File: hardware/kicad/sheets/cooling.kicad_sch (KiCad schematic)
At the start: 22 parts, among them J3 FAN (4-pin PWM), J4 PUMP (4-pin PWM), J5 ALPHACOOL ES FLOW (3-pin), J6 ALPHACOOL ES NTC 10k, U10 EMC2303-x-KP

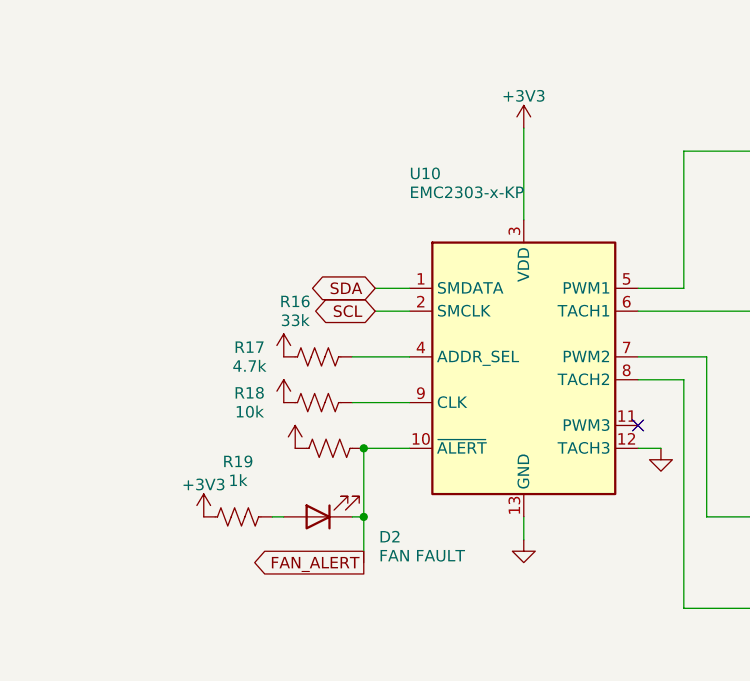
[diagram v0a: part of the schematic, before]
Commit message: Put supply pins on top and grounds on the bottom of IC symbols; flake8-clean Python
Schematic: re-laid out pins on U2, U3, U6, U7, U11, U14, U17-U20, U22-U24
and PS1 (supply on top, ground/strap pins on the bottom edge) via custom
`cryocooler:` symbols (make_lib.from_stock) and a gnd_bus helper; U18/U2
use mirroring instead of a 180 degree rotation. Nets are unchanged (ERC 0,
117/117 datasheet rules, PCB nets still match). Text placement now shows
every power-symbol name, avoids wires, and uses a realistic character width.

Python: black -l 79 -S plus manual wrapping so hardware/kicad and scripts/
pass flake8; add .flake8.

Co-Authored-By: Claude Sonnet 5.5 <noreply@anthropic.com>
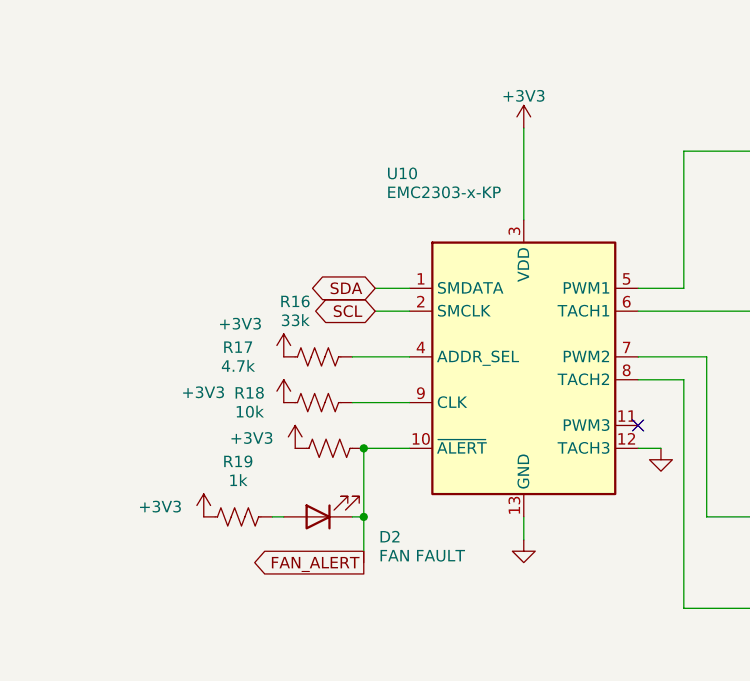
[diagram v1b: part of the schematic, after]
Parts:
- removed C28: 100nF, Capacitor_SMD:C_0603_1608Metric, symbol Device:C
- removed D2: FAN FAULT, LED_SMD:LED_0603_1608Metric, symbol Device:LED
- removed J3: FAN (4-pin PWM), Connector_Molex:Molex_KK-254_AE-6410-04A_1x04_P2.54mm_Vertical, symbol Connector_Generic:Conn_01x04
- removed R21, R23: 4.7k, Resistor_SMD:R_0603_1608Metric, symbol Device:R_US
- removed R25: 10k, Resistor_SMD:R_0603_1608Metric, symbol Device:R_US
- added C25: 100nF, Capacitor_SMD:C_0603_1608Metric, symbol Device:C
- added J5: ALPHACOOL ES FLOW (3-pin), Connector_Molex:Molex_KK-254_AE-6410-03A_1x03_P2.54mm_Vertical, symbol Connector_Generic:Conn_01x03
- added R19: 1k, Resistor_SMD:R_0603_1608Metric, symbol Device:R_US
- added R20, R22, R26: 10k, Resistor_SMD:R_0603_1608Metric, symbol Device:R_US
- C28: renamed from R26; value 10k -> 100nF; footprint Resistor_SMD:R_0603_1608Metric -> Capacitor_SMD:C_0603_1608Metric; symbol Device:R_US -> Device:C
- D2: renamed from R18; value 10k -> FAN FAULT; footprint Resistor_SMD:R_0603_1608Metric -> LED_SMD:LED_0603_1608Metric; symbol Device:R_US -> Device:LED
- J3: renamed from R19; value 1k -> FAN (4-pin PWM); footprint Resistor_SMD:R_0603_1608Metric -> Connector_Molex:Molex_KK-254_AE-6410-04A_1x04_P2.54mm_Vertical; symbol Device:R_US -> Connector_Generic:Conn_01x04
- R16: renamed from C25; value 100nF -> 33k; footprint Capacitor_SMD:C_0603_1608Metric -> Resistor_SMD:R_0603_1608Metric; symbol Device:C -> Device:R_US
- R17: renamed from R16; value 33k -> 4.7k
- R18: renamed from R17; value 4.7k -> 10k
- R21: renamed from R20; value 10k -> 4.7k
- R23: renamed from R22; value 10k -> 4.7k
- R25: renamed from J5; value ALPHACOOL ES FLOW (3-pin) -> 10k; footprint Connector_Molex:Molex_KK-254_AE-6410-03A_1x03_P2.54mm_Vertical -> Resistor_SMD:R_0603_1608Metric; symbol Connector_Generic:Conn_01x03 -> Device:R_US
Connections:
- net +12V: now also J3.2 (Pin_2), J5.2 (Pin_2); no longer R25.2 (Pin_2)
- net +3V3: now also R25.1, C25.1, R19.1, R20.1, R22.1, R26.1; no longer C28.1, D2.1, J3.1
- net FAN_ALERT: now also D2.1 (K), R18.2; no longer D2.2
- net FLOW_TACH: now also R25.2
- net GND: now also C28.2, J3.1 (Pin_1), C25.2, J5.1 (Pin_1); no longer R16.2, R25.1 (Pin_1)
- net NTC_ADC: now also C28.1, R26.2; no longer C28.2
- net at R24.2: now also J5.3 (Pin_3); no longer R25.3 (Pin_3)
- net at R21.2: now also J3.3 (Pin_3), U10.6 (TACH1); no longer U10.5 (PWM1)
- net at U10.4 (ADDR_SEL): now also R16.2; no longer R17.2
- net at J4.4 (Pin_4), U10.7 (PWM2): now also R22.2; no longer R23.2
- net at J4.3 (Pin_3), U10.8 (TACH2): now also R23.2
- net at U10.9 (CLK): now also R17.2; no longer R18.2
- new net: D2.2 (A), R19.2
- new net: J3.4 (Pin_4), R20.2, U10.5 (PWM1)
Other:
- moved on the sheet: D2, R17, R18, R21, R23

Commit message: KiCad schematic: INA239, ADS1220, SC18IS604 bridge, relay driver, test points
- system_current: INA237 -> INA239 (SPI, CS GPIO3) with the 49.9 ohm / 470 nF
  input filter, power LED and ALERT LED; VBUS shares the filtered IN- node.
- cold_head: ADS122C04 -> ADS1220 (SPI, CS GPIO44).
- i2c_bridge (new): SC18IS604 SPI-to-I2C bridge for the EMC2303, with a
  74LVC1G125 gating its MISO onto the shared bus.
- compressor_relay (new): GPIO16 high-side switch sharing one generator
  function with the amplifier REM switch.
- debug (new): about 40 test points and rail LEDs (the isolated rail LED
  returns to ISO_GND).
- ISO7741 -> ACS37800 SPI lines are straight wires (pins reordered on the
  symbol); USB_VBUS is one wire plus a naming label.
- Custom symbols for INA239, ADS1220, SC18IS604; datasheet rules 117 -> 162;
  GPIO map checks updated. ERC 0.

Co-Authored-By: Claude Sonnet 5.5 <noreply@anthropic.com>
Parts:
- removed C24: 1uF, Capacitor_SMD:C_0805_2012Metric, symbol Device:C
- removed J5: ALPHACOOL ES FLOW (3-pin), Connector_Molex:Molex_KK-254_AE-6410-03A_1x03_P2.54mm_Vertical, symbol Connector_Generic:Conn_01x03
- removed J6: ALPHACOOL ES NTC 10k, Connector_JST:JST_XH_B2B-XH-A_1x02_P2.50mm_Vertical, symbol Connector_Generic:Conn_01x02
- removed R18, R20, R26: 10k, Resistor_SMD:R_0603_1608Metric, symbol Device:R_US
- added C25: 100nF, Capacitor_SMD:C_0603_1608Metric, symbol Device:C
- added C26, C27: 22uF/25V, Capacitor_SMD:C_1210_3225Metric, symbol Device:C
- added R14: 33k, Resistor_SMD:R_0603_1608Metric, symbol Device:R_US
- added R17: 1k, Resistor_SMD:R_0603_1608Metric, symbol Device:R_US
- added U10: EMC2303-x-KP, Package_DFN_QFN:VQFN-12-1EP_4x4mm_P0.8mm_EP2.1x2.1mm_ThermalVias, symbol Driver_Motor:EMC2303-x-KP
- C24: renamed from U10; value EMC2303-x-KP -> 1uF; footprint Package_DFN_QFN:VQFN-12-1EP_4x4mm_P0.8mm_EP2.1x2.1mm_ThermalVias -> Capacitor_SMD:C_0805_2012Metric; symbol Driver_Motor:EMC2303-x-KP -> Device:C
- D2: renamed from R17; value 4.7k -> FAN FAULT; footprint Resistor_SMD:R_0603_1608Metric -> LED_SMD:LED_0603_1608Metric; symbol Device:R_US -> Device:LED
- J5: renamed from C27; value 22uF/25V -> ALPHACOOL ES FLOW (3-pin); footprint Capacitor_SMD:C_1210_3225Metric -> Connector_Molex:Molex_KK-254_AE-6410-03A_1x03_P2.54mm_Vertical; symbol Device:C -> Connector_Generic:Conn_01x03
- J6: renamed from R25; value 10k -> ALPHACOOL ES NTC 10k; footprint Resistor_SMD:R_0603_1608Metric -> Connector_JST:JST_XH_B2B-XH-A_1x02_P2.50mm_Vertical; symbol Device:R_US -> Connector_Generic:Conn_01x02
- R15: renamed from C25; value 100nF -> 4.7k; footprint Capacitor_SMD:C_0603_1608Metric -> Resistor_SMD:R_0603_1608Metric; symbol Device:C -> Device:R_US
- R16: value 33k -> 10k
- R18: renamed from D2; value FAN FAULT -> 10k; footprint LED_SMD:LED_0603_1608Metric -> Resistor_SMD:R_0603_1608Metric; symbol Device:LED -> Device:R_US
- R19: value 1k -> 4.7k
- R20: renamed from C26; value 22uF/25V -> 10k; footprint Capacitor_SMD:C_1210_3225Metric -> Resistor_SMD:R_0603_1608Metric; symbol Device:C -> Device:R_US
- R22: value 10k -> 1k
- R23: value 4.7k -> 10k
- R24: value 1k -> 10k
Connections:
- net +12V: now also J5.2 (Pin_2), C26.1, C27.1; no longer J5.1, R20.1
- net +3V3: now also C24.1, R18.1, R20.1, R24.1, C25.1, R14.1, R17.1, U10.3 (VDD); no longer C24.3 (VDD), D2.1, J6.1, R22.1
- net FAN_ALERT: now also D2.1 (K), R16.2, U10.10 (~{ALERT}); no longer C24.10 (~{ALERT}), R18.1 (K)
- net FLOW_TACH: now also R22.1, R23.2; no longer J6.2, R24.1
- net GND: now also C24.2, J5.1 (Pin_1), J6.2 (Pin_2), C25.2, C26.2, C27.2, U10.12 (TACH3), U10.13 (GND); no longer C24.12 (TACH3), C24.13 (GND), J5.2, R15.2, R20.2
- net NTC_ADC: now also J6.1 (Pin_1), R24.2
- net SCL: now also U10.2 (SMCLK); no longer C24.2 (SMCLK)
- net SDA: now also U10.1 (SMDATA); no longer C24.1 (SMDATA)
- net at R19.2: now also J3.3 (Pin_3), U10.6 (TACH1); no longer R18.2 (A)
- net at J3.4 (Pin_4): now also R18.2, U10.5 (PWM1); no longer C24.5 (PWM1)
- net at D2.2 (A): now also R17.2; no longer C24.9 (CLK)
- new net: J4.3 (Pin_3), R21.2, U10.8 (TACH2)
- new net: J4.4 (Pin_4), R20.2, U10.7 (PWM2)
- new net: J5.3 (Pin_3), R22.2
- new net: R14.2, U10.4 (ADDR_SEL)
- new net: R15.2, U10.9 (CLK)
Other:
- moved on the sheet: D2, R16, R18

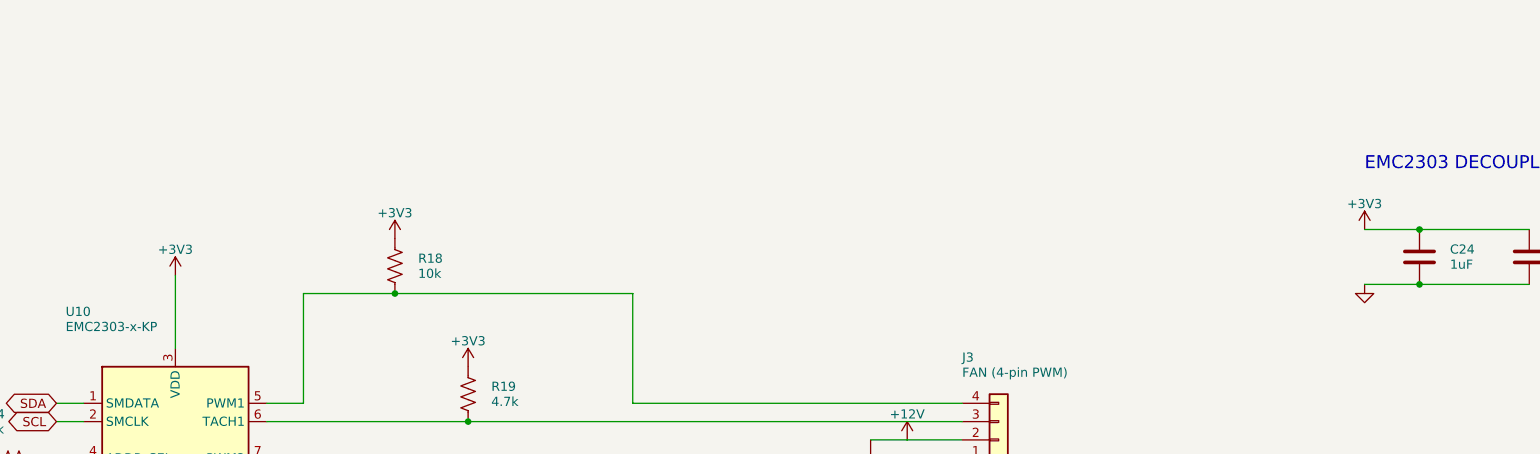
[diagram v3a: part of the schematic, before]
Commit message: Add per-section supply jumpers, 8-pin IMU header and connector pin labels
- Four 1.27 mm 2-pin jumpers (JP1-JP4), each with a rail-on LED, cut the
  supply of one section for debugging: signal generator +3V3, +-15V
  generator +5V in, isolated amp-current supply +5V in, and a shared
  +3V3 net for the cooling chips (EMC2303, RTD ADC, I2C bridge).
- J14 is now an 8-pin JST XH in the Adafruit LSM6DSOX pad order
  (VIN, GND, SCL, SDA, DO, CS, I1, I2); firmware pin comments updated.
- Pin-function labels beside every connector, "RAILS ±15V" box title.
- Board re-placed and re-routed (130 x 110 mm); DRC 0 errors, 0 unconnected,
  ERC 0, 173 datasheet rules pass. BOM, READMEs, Gerbers and renders
  regenerated; link_usb_vbus.py now adapts to the routed layout.

Co-Authored-By: Claude Sonnet 5.5 <noreply@anthropic.com>
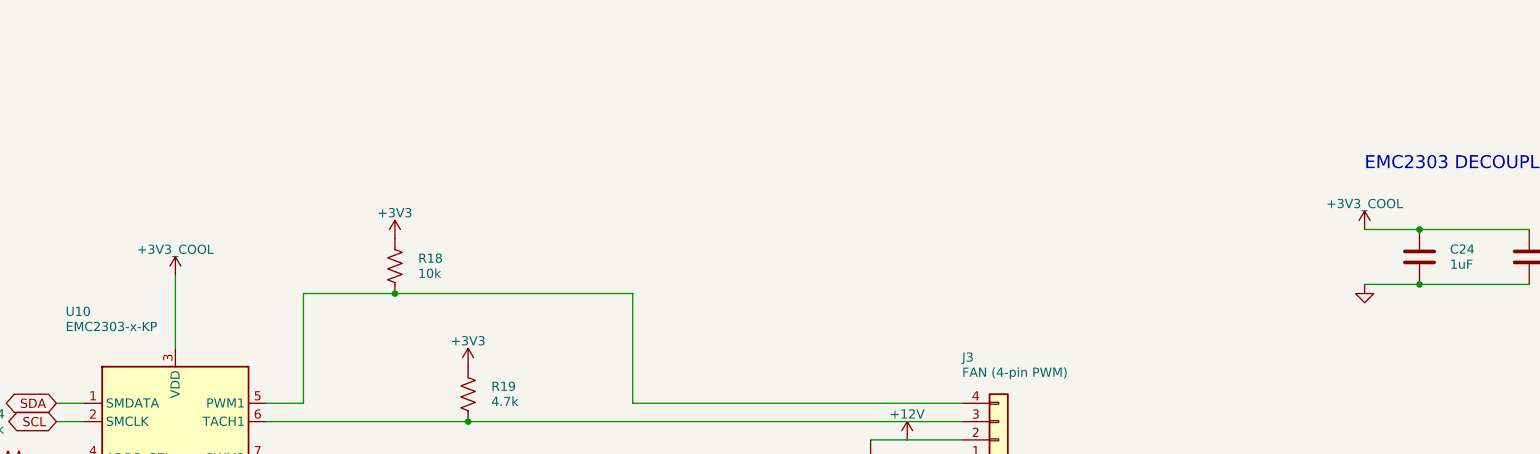
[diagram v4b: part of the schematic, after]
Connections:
- net +3V3: no longer C24.1, C25.1, U10.3 (VDD)
- new net +3V3_COOL: C24.1, C25.1, U10.3 (VDD)
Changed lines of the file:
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@@
 	)
 	(junction
-		(at 106.68 190.5)
+		(at 132.08 116.84)
 		(diameter 0)
 		(color 0 0 0 0)
 	)
 	(junction
-		(at 132.08 116.84)
+		(at 106.68 190.5)
 		(diameter 0)
 		(color 0 0 0 0)
 	)
 	(junction
-		(at 106.68 66.04)
+		(at 58.42 106.68)
 		(diameter 0)
 		(color 0 0 0 0)
 	)
 	(junction
-		(at 116.84 83.82)
+		(at 248.92 57.15)
 		(diameter 0)
 		(color 0 0 0 0)
 	)
 	(junction
-		(at 248.92 57.15)
+		(at 58.42 99.06)
 		(diameter 0)
 		(color 0 0 0 0)
 	)
 	(junction
-		(at 58.42 106.68)
+		(at 248.92 64.77)
 		(diameter 0)
 		(color 0 0 0 0)
 	)
 	(junction
-		(at 114.3 106.68)
+		(at 109.22 160.02)
 		(diameter 0)
 		(color 0 0 0 0)
 	)
 	(junction
-		(at 58.42 99.06)
+		(at 116.84 83.82)
 		(diameter 0)
 		(color 0 0 0 0)
 	)
 	(junction
-		(at 109.22 160.02)
+		(at 106.68 66.04)
 		(diameter 0)
 		(color 0 0 0 0)
 	)
 	(junction
-		(at 116.84 190.5)
+		(at 114.3 106.68)
 		(diameter 0)
 		(color 0 0 0 0)
 	)
 	(junction
-		(at 248.92 64.77)
+		(at 116.84 190.5)
 		(diameter 0)
 		(color 0 0 0 0)
@@
 	(wire
 		(pts
-			(xy 152.4 114.3) (xy 185.42 114.3)
+			(xy 93.98 116.84) (xy 132.08 116.84)
 		)
 		(stroke
@@
 	(wire
 		(pts
-			(xy 59.69 81.28) (xy 63.5 81.28)
+			(xy 152.4 114.3) (xy 185.42 114.3)
 		)
 		(stroke
@@
 	(wire
 		(pts
-			(xy 172.72 119.38) (xy 177.8 119.38)
+			(xy 116.84 190.5) (xy 134.62 190.5)
 		)
 		(stroke
@@
 	(wire
 		(pts
-			(xy 241.3 57.15) (xy 248.92 57.15)
+			(xy 109.22 160.02) (xy 119.38 160.02)
 		)
 		(stroke
@@
 	(wire
 		(pts
-			(xy 182.88 88.9) (xy 185.42 88.9)
+			(xy 248.92 57.15) (xy 264.16 57.15)
 		)
 		(stroke
@@
 	(wire
 		(pts
-			(xy 127 160.02) (xy 134.62 160.02)
+			(xy 116.84 83.82) (xy 185.42 83.82)
 		)
 		(stroke
@@
 	(wire
 		(pts
-			(xy 76.2 106.68) (xy 76.2 109.22)
+			(xy 93.98 66.04) (xy 93.98 81.28)
 		)
 		(stroke
@@
 	(wire
 		(pts
-			(xy 182.88 121.92) (xy 185.42 121.92)
+			(xy 76.2 106.68) (xy 76.2 109.22)
 		)
 		(stroke
@@
 	(wire
 		(pts
-			(xy 124.46 154.94) (xy 134.62 154.94)
+			(xy 58.42 99.06) (xy 58.42 106.68)
 		)
 		(stroke
@@
 	(wire
 		(pts
-			(xy 58.42 99.06) (xy 63.5 99.06)
+			(xy 248.92 64.77) (xy 264.16 64.77)
 		)
 		(stroke
@@
 	(wire
 		(pts
-			(xy 114.3 106.68) (xy 152.4 106.68)
+			(xy 96.52 190.5) (xy 106.68 190.5)
 		)
 		(stroke
@@
 	(wire
 		(pts
-			(xy 109.22 160.02) (xy 119.38 160.02)
+			(xy 58.42 106.68) (xy 58.42 111.76)
 		)
 		(stroke
@@
 	(wire
 		(pts
-			(xy 139.7 66.04) (xy 139.7 81.28)
+			(xy 241.3 57.15) (xy 248.92 57.15)
 		)
 		(stroke
@@
 	(wire
 		(pts
-			(xy 116.84 190.5) (xy 134.62 190.5)
+			(xy 93.98 91.44) (xy 93.98 116.84)
 		)
 		(stroke
@@
 	(wire
 		(pts
-			(xy 152.4 106.68) (xy 152.4 114.3)
+			(xy 58.42 99.06) (xy 63.5 99.06)
 		)
 		(stroke
@@
 	(wire
 		(pts
-			(xy 129.54 157.48) (xy 134.62 157.48)
+			(xy 139.7 81.28) (xy 185.42 81.28)
 		)
 		(stroke
@@
 	(wire
 		(pts
-			(xy 96.52 106.68) (xy 114.3 106.68)
+			(xy 152.4 106.68) (xy 152.4 114.3)
 		)
 		(stroke
@@
 	(wire
 		(pts
-			(xy 241.3 64.77) (xy 248.92 64.77)
+			(xy 48.26 106.68) (xy 49.53 106.68)
 		)
 		(stroke
@@
 	(wire
 		(pts
-			(xy 88.9 99.06) (xy 91.44 99.06)
+			(xy 241.3 64.77) (xy 248.92 64.77)
 		)
 		(stroke
@@
 	(wire
 		(pts
-			(xy 93.98 66.04) (xy 106.68 66.04)
+			(xy 177.8 86.36) (xy 185.42 86.36)
 		)
 		(stroke
@@
 	(wire
 		(pts
-			(xy 76.2 63.5) (xy 76.2 73.66)
+			(xy 124.46 154.94) (xy 134.62 154.94)
 		)
 		(stroke
@@
 	(wire
 		(pts
-			(xy 106.68 190.5) (xy 116.84 190.5)
+			(xy 114.3 106.68) (xy 152.4 106.68)
 		)
 		(stroke
@@
 	(wire
 		(pts
-			(xy 88.9 81.28) (xy 93.98 81.28)
+			(xy 57.15 106.68) (xy 58.42 106.68)
 		)
 		(stroke
@@
 	(wire
 		(pts
-			(xy 59.69 83.82) (xy 63.5 83.82)
+			(xy 88.9 83.82) (xy 116.84 83.82)
 		)
 		(stroke
@@
 	(wire
 		(pts
-			(xy 139.7 81.28) (xy 185.42 81.28)
+			(xy 88.9 81.28) (xy 93.98 81.28)
 		)
 		(stroke
@@
 	(wire
 		(pts
-			(xy 88.9 88.9) (xy 96.52 88.9)
+			(xy 172.72 119.38) (xy 177.8 119.38)
 		)
 		(stroke
@@
 	(wire
 		(pts
-			(xy 96.52 160.02) (xy 109.22 160.02)
+			(xy 106.68 66.04) (xy 139.7 66.04)
 		)
 		(stroke
@@
 	(wire
 		(pts
-			(xy 106.68 66.04) (xy 139.7 66.04)
+			(xy 106.68 190.5) (xy 116.84 190.5)
 		)
 		(stroke
@@
 	(wire
 		(pts
-			(xy 93.98 116.84) (xy 132.08 116.84)
+			(xy 172.72 86.36) (xy 177.8 86.36)
 		)
 		(stroke
@@
 	(wire
 		(pts
-			(xy 96.52 88.9) (xy 96.52 106.68)
+			(xy 129.54 157.48) (xy 134.62 157.48)
 		)
 		(stroke
@@
 	(wire
 		(pts
-			(xy 58.42 106.68) (xy 58.42 111.76)
+			(xy 139.7 66.04) (xy 139.7 81.28)
 		)
 		(stroke
@@
 	(wire
 		(pts
-			(xy 132.08 193.04) (xy 134.62 193.04)
+			(xy 88.9 99.06) (xy 91.44 99.06)
 		)
 		(stroke
@@
 	(wire
 		(pts
-			(xy 132.08 116.84) (xy 185.42 116.84)
+			(xy 76.2 63.5) (xy 76.2 73.66)
 		)
 		(stroke
@@
 	(wire
 		(pts
-			(xy 96.52 190.5) (xy 106.68 190.5)
+			(xy 96.52 88.9) (xy 96.52 106.68)
 		)
 		(stroke
@@
 	(wire
 		(pts
-			(xy 48.26 106.68) (xy 49.53 106.68)
+			(xy 127 160.02) (xy 134.62 160.02)
 		)
 		(stroke
@@
 	(wire
 		(pts
-			(xy 248.92 57.15) (xy 264.16 57.15)
+			(xy 93.98 66.04) (xy 106.68 66.04)
 		)
 		(stroke
@@
 	(wire
 		(pts
-			(xy 93.98 66.04) (xy 93.98 81.28)
+			(xy 96.52 160.02) (xy 109.22 160.02)
 		)
 		(stroke
@@
 	(wire
 		(pts
-			(xy 57.15 106.68) (xy 58.42 106.68)
+			(xy 88.9 88.9) (xy 96.52 88.9)
 		)
 		(stroke
@@
 	(wire
 		(pts
-			(xy 116.84 83.82) (xy 185.42 83.82)
+			(xy 59.69 83.82) (xy 63.5 83.82)
 		)
 		(stroke
@@
 	(wire
 		(pts
-			(xy 172.72 86.36) (xy 177.8 86.36)
+			(xy 132.08 193.04) (xy 134.62 193.04)
 		)
 		(stroke
@@
 	(wire
 		(pts
-			(xy 57.15 88.9) (xy 63.5 88.9)
+			(xy 182.88 121.92) (xy 185.42 121.92)
 		)
 		(stroke
@@
 	(wire
 		(pts
-			(xy 58.42 99.06) (xy 58.42 106.68)
+			(xy 59.69 81.28) (xy 63.5 81.28)
 		)
 		(stroke
@@
 	(wire
 		(pts
-			(xy 93.98 91.44) (xy 93.98 116.84)
+			(xy 182.88 88.9) (xy 185.42 88.9)
 		)
 		(stroke
@@
 	(wire
 		(pts
-			(xy 177.8 86.36) (xy 185.42 86.36)
+			(xy 57.15 88.9) (xy 63.5 88.9)
 		)
 		(stroke
@@
 	(wire
 		(pts
-			(xy 177.8 119.38) (xy 185.42 119.38)
+			(xy 57.15 93.98) (xy 63.5 93.98)
 		)
 		(stroke
@@
 	(wire
 		(pts
-			(xy 248.92 64.77) (xy 264.16 64.77)
+			(xy 177.8 119.38) (xy 185.42 119.38)
 		)
 		(stroke
@@
 	(wire
 		(pts
-			(xy 88.9 83.82) (xy 116.84 83.82)
+			(xy 88.9 91.44) (xy 93.98 91.44)
 		)
 		(stroke
@@
 	(wire
 		(pts
-			(xy 88.9 91.44) (xy 93.98 91.44)
+			(xy 132.08 116.84) (xy 185.42 116.84)
 		)
 		(stroke
@@
 	(wire
 		(pts
-			(xy 57.15 93.98) (xy 63.5 93.98)
+			(xy 96.52 106.68) (xy 114.3 106.68)
 		)
 		(stroke
@@
 			)
 		)
-		(property "Value" "+3V3"
+		(property "Value" "+3V3_COOL"
 			(at 76.2 59.944 0)
 			(show_name no)
@@
 			)
 		)
-		(property "Value" "+3V3"
+		(property "Value" "+3V3_COOL"
 			(at 241.3 53.594 0)
 			(show_name no)
